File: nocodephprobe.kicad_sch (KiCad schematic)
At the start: 44 parts, among them J1 BNC (pH Probe), J2 10K, Q1 2N7002, SW1 SW_SPST, U1 TLV272, U2 ICL7106CPL, U3 MCP1501T-10E/CHY, U4 VI-302-DP-RC-S

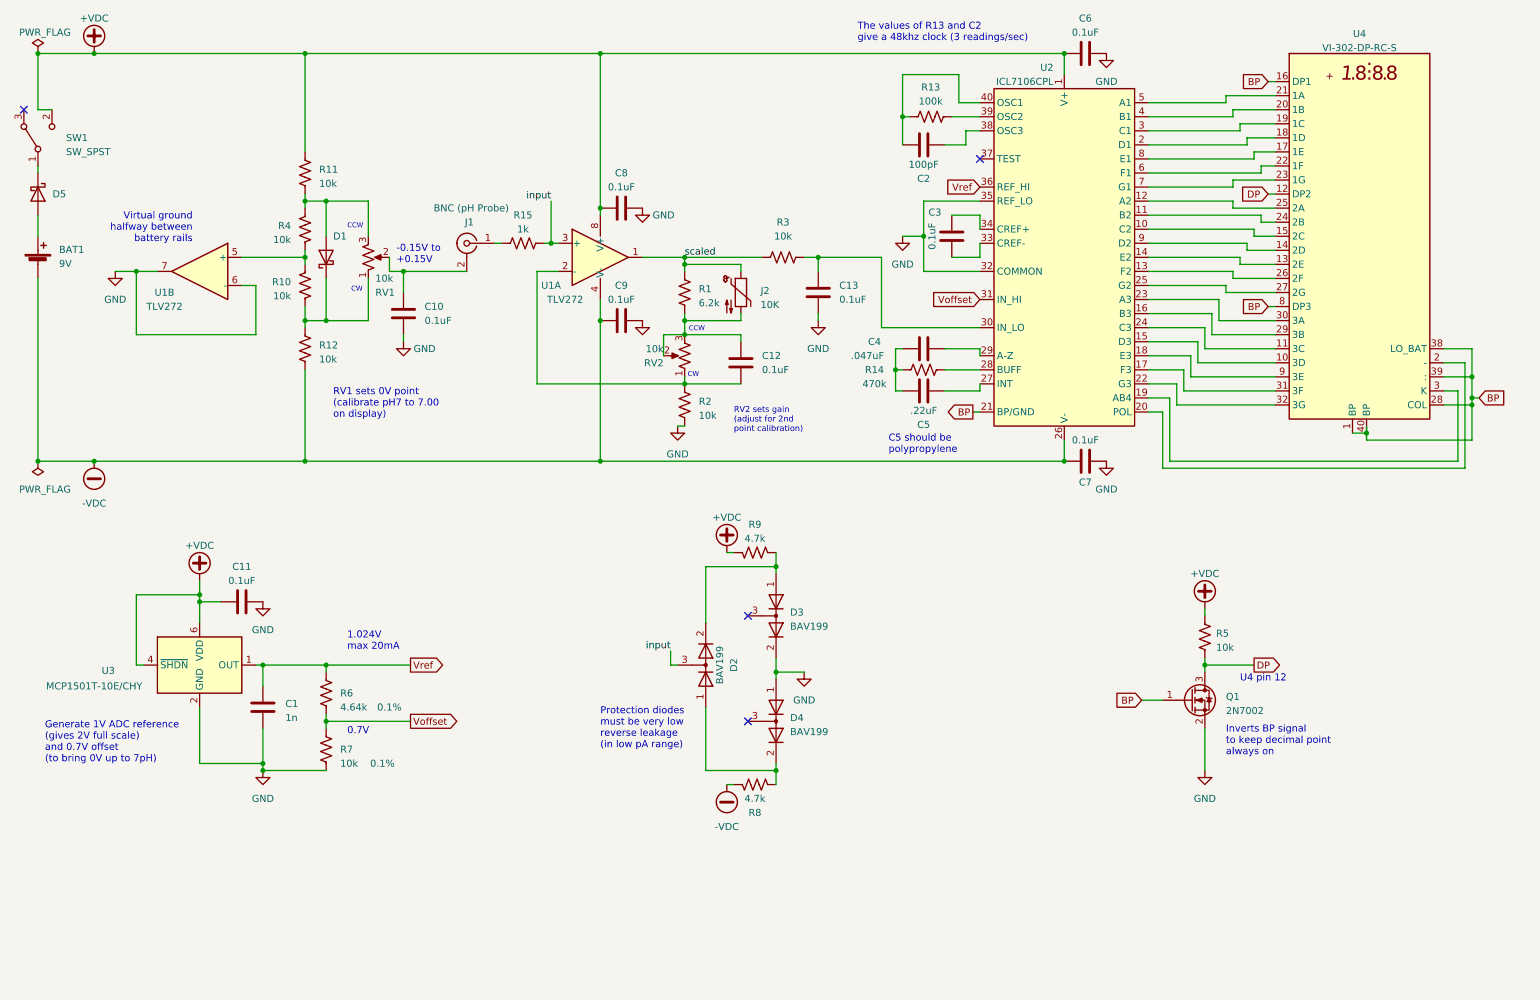
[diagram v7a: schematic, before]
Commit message: Low battery indicator
This change adds a comparator and xor gate to implement a low-battery
indicator. When the positive rail goes below about 3V, then the output
of U5A goes high. The output of U5A is XOR'd with the backplane which
inverts the backplane when it is high, turning on the LOBAT LCD
indicator.

I'm using the spare coparator to replace the 2n7002 to keep the decimal
point on.

I got this all layed out on the PCB, but I'm increasingly unhappy with
how stringy the VDC+ trace is becoming. I think I will try laying it out
as a 4-layer board.
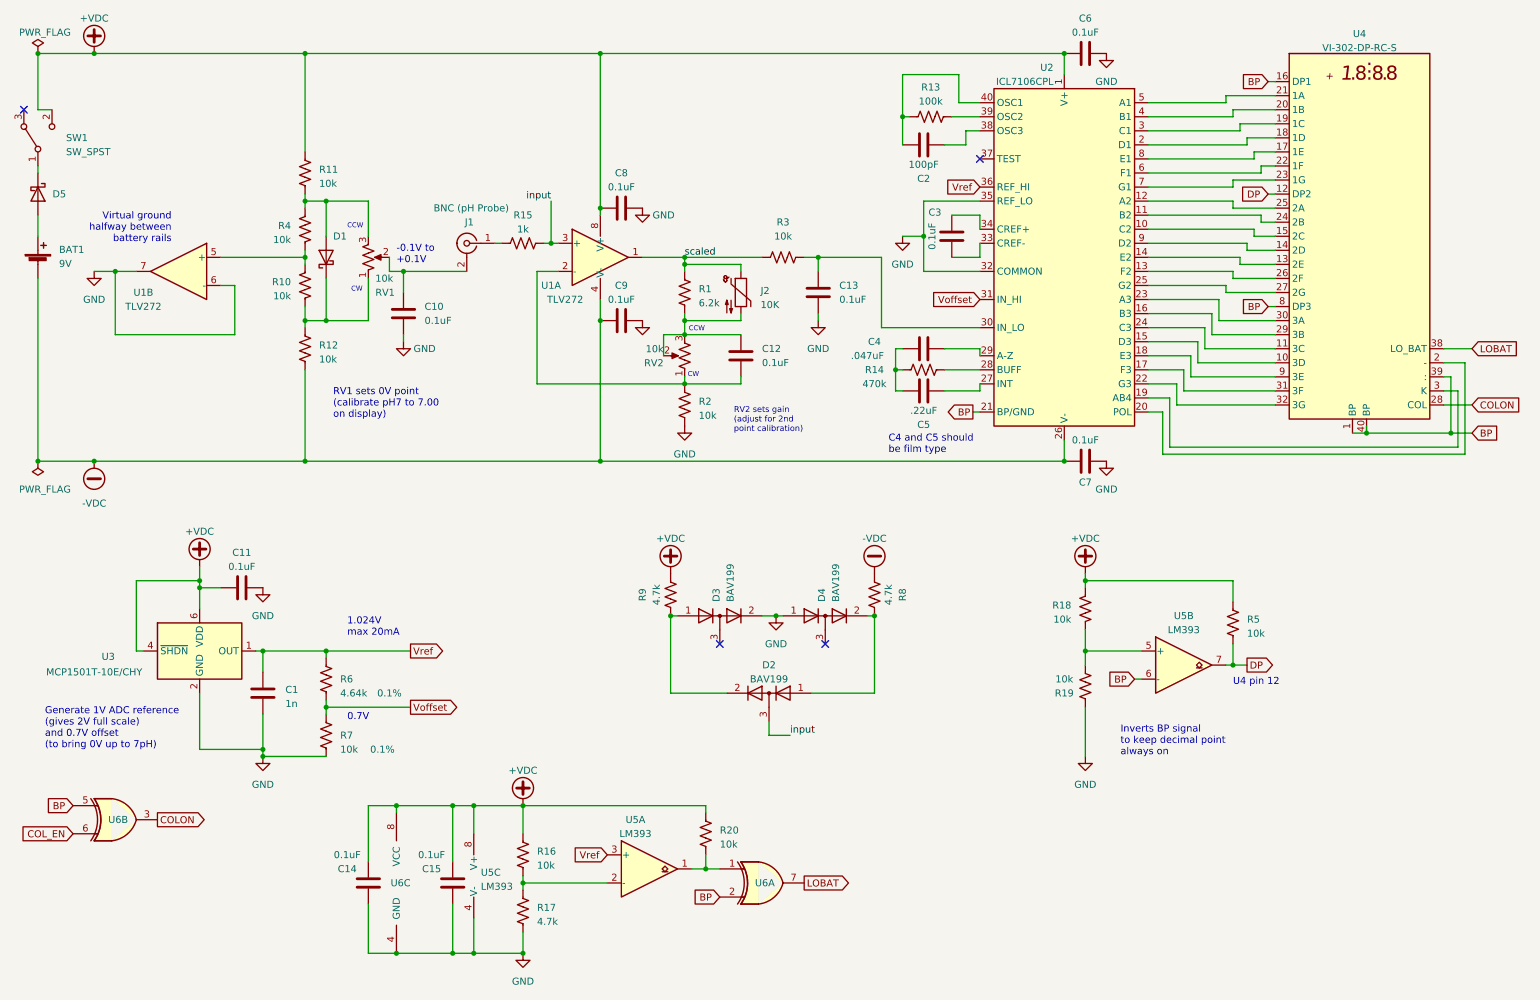
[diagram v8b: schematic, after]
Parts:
- removed Q1: 2N7002, Package_TO_SOT_SMD:SOT-23, symbol Transistor_FET:2N7002
- added C14, C15: 0.1uF, Capacitor_SMD:C_0805_2012Metric_Pad1.18x1.45mm_HandSolder, symbol Device:C
- added R16, R18, R19, R20: 10k, Resistor_SMD:R_0805_2012Metric_Pad1.20x1.40mm_HandSolder, symbol Device:R_US
- added R17: 4.7k, Resistor_SMD:R_0805_2012Metric_Pad1.20x1.40mm_HandSolder, symbol Device:R_US
- added U5: LM393, Package_SO:TSSOP-8_4.4x3mm_P0.65mm, symbol Comparator:LM393
- added U6: 74HC2G86, Package_SO:TSSOP-8_3x3mm_P0.65mm, symbol Custom:74HC2G86
- SW1: pn (none) -> MTS-102
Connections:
- net +VDC: now also C14.1, C15.1, R16.2, R18.1, R20.2, U5.8 (V+), U6.8 (VCC)
- net BP: now also U5.6 (-), U6.2, U6.5; no longer U4.28 (COL), U4.38 (LO_BAT)
- net DP: now also U5.7
- net GND: now also C14.2, C15.2, R17.1, R19.2, U5.4 (V-), U6.4 (GND)
- net Vref: now also U5.3 (+)
- new net: R20.1, U5.1, U6.1
- new net: R16.1, R17.2, U5.2 (-)
- new net: R18.2, R19.1, U5.5 (+)
- new net COLON: U4.28 (COL), U6.3
- new net COL_EN: U6.6
- new net LOBAT: U4.38 (LO_BAT), U6.7
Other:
- note added: "-0.1V to +0.1V"
- note added: "C4 and C5 should be film type"
- note removed: "-0.15V to +0.15V"
- note removed: "C5 should be polypropylene"
- note removed: "Protection diodes must be very low reverse leakage (in low pA range)"
- note removed: "The values of R13 and C2 give a 48khz clock (3 readings/sec)"
- moved on the sheet: C1, C11, C12, D2, D3, D4, R6, R7, R8, R9, U1B, U3
